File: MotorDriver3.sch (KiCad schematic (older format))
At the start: 38 parts, among them J22 43045-0802, J23 53426-0410, U45 MAX40056FAUA+, U46 DRV8312DDWR, U47 MAX40056FAUA+, U48 MIC2090-2YM5-TR

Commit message: PVT
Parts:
- C183: renamed from C191; footprint Capacitor-Chip:C_CHIP_1608_Reflow -> Capacitor-Chip:C_CHIP_1005_Hand_NoSilk; PartName GRM188R61E105KA12D -> TMK105BJ105MV-F
- C184: renamed from C192; PartName C1005X5R1V105K050BE -> TMK105BJ105MV-F
- C185: renamed from C193; PartName C1005X5R1V105K050BE -> TMK105BJ105MV-F
- C186: renamed from C194; footprint Capacitor-Chip:C_CHIP_1608_Reflow -> Capacitor-Chip:C_CHIP_1005_Hand_NoSilk; PartName GRM188R61E105KA12D -> TMK105BJ105MV-F
- C187: renamed from C195; footprint Capacitor-Chip:C_CHIP_1608_Reflow -> Capacitor-Chip:C_CHIP_1005_Hand_NoSilk; PartName GRM188R61E105KA12D -> TMK105BJ105MV-F
- C188: renamed from C196; footprint Capacitor-Chip:C_CHIP_1608_Reflow -> Capacitor-Chip:C_CHIP_1005_Hand_NoSilk; PartName GRM188R61E105KA12D -> TMK105BJ105MV-F
- C190: renamed from C198; PartName C1005X5R1V105K050BE -> TMK105BJ105MV-F
- C191: renamed from C199; PartName C1005X5R1V105K050BE -> TMK105BJ105MV-F
- C199: renamed from C207; PartName C1005X5R1V105K050BE -> TMK105BJ105MV-F
- R102: renamed from R117; value 2m -> 3m; PartName PMR18EZPJV2L0 -> PMR18EZPFV3L00
- R103: renamed from R118; value 2m -> 3m; PartName PMR18EZPJV2L0 -> PMR18EZPFV3L00
- renumbered C197 to C189, C200 to C192, C201 to C193, C202 to C194, C203 to C195, C204 to C196, C205 to C197, C206 to C198, L19 to L15, L20 to L16, L21 to L17, R115 to R100, R116 to R101, R119 to R104, R120 to R105, R113 to R98, R114 to R99, RA24 to RA25, RA25 to RA26, RA26 to RA27, U45 to U42, U46 to U43, U47 to U44, U48 to U45

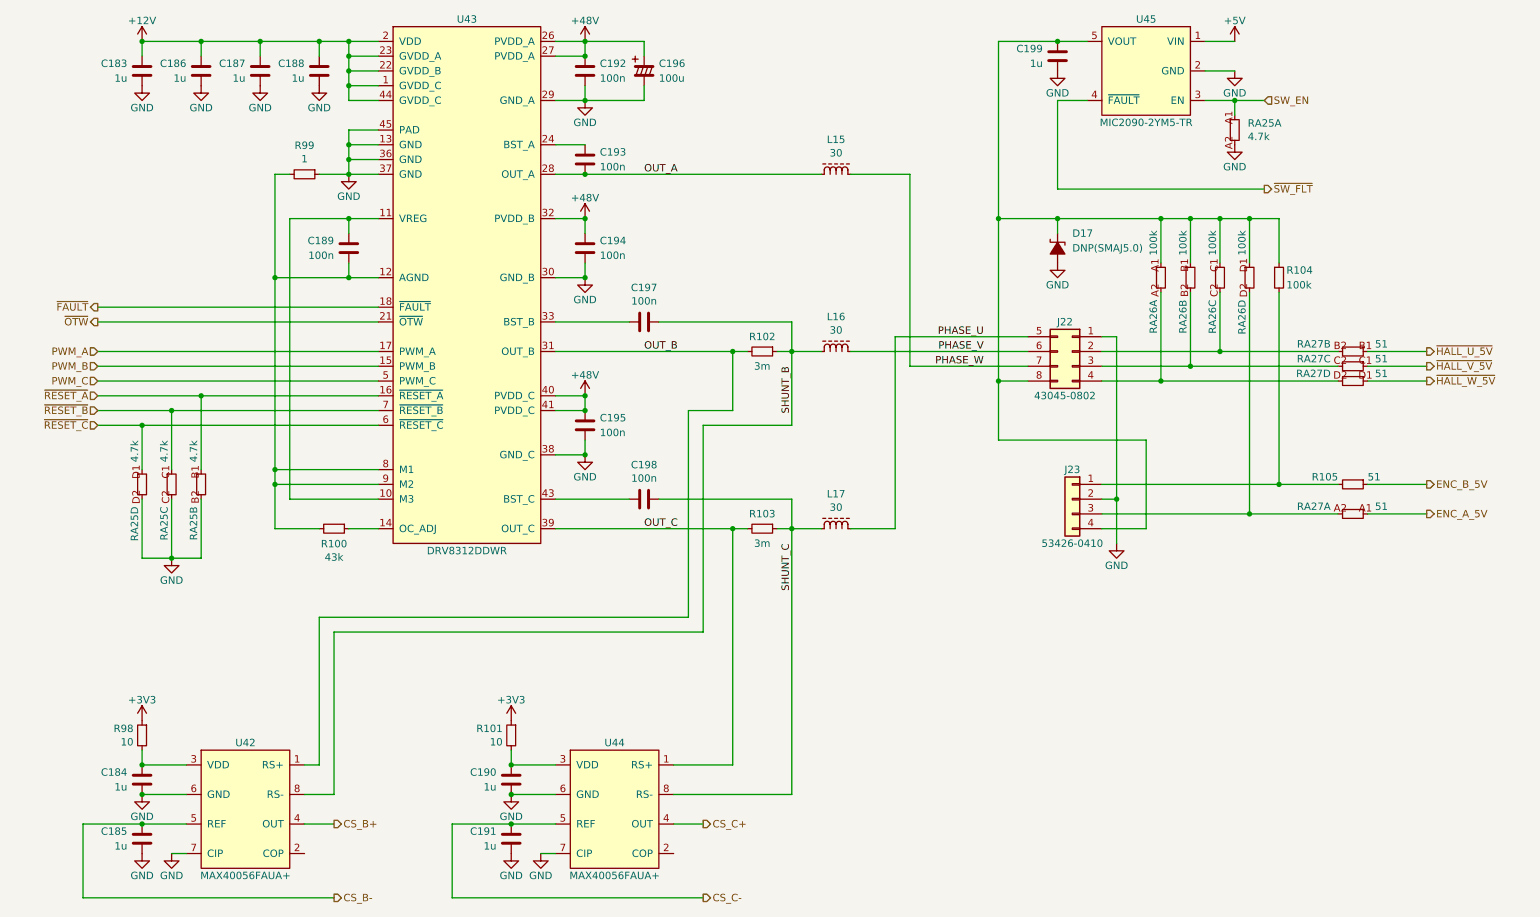
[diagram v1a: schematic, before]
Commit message: SBUにTVSダイオードを追加
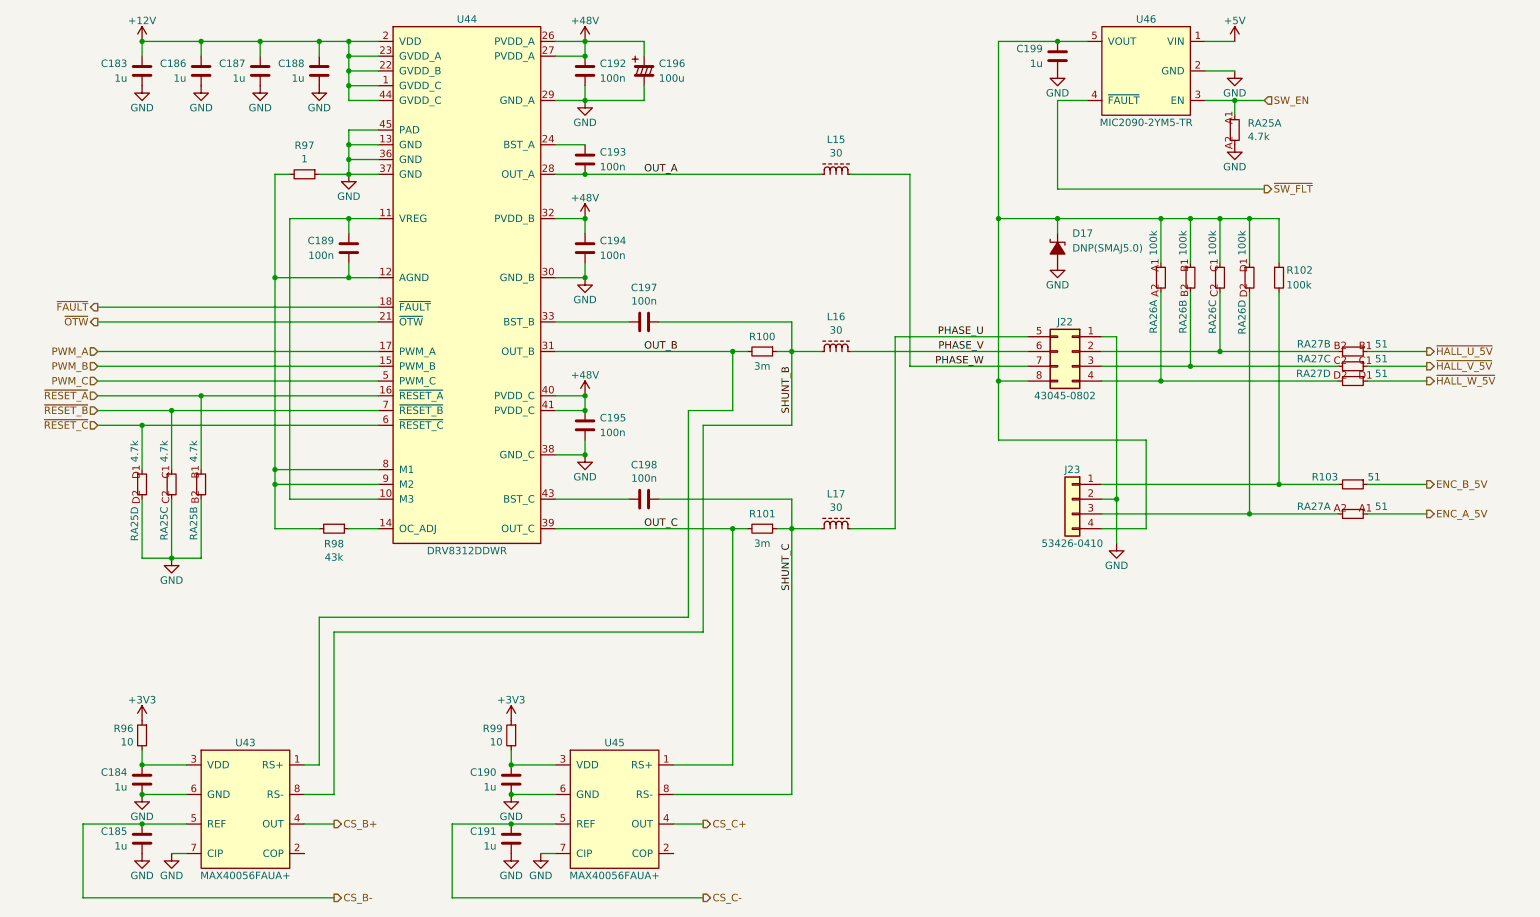
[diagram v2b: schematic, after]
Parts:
- renumbered R102 to R100, R103 to R101, R104 to R102, R105 to R103, R98 to R96, R99 to R97, R100 to R98, R101 to R99, U42 to U43, U43 to U44, U44 to U45, U45 to U46
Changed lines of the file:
@@
 AR Path="/5F237486/5E603889" Ref="U?"  Part="1"
 AR Path="/5F259EEE/5E603889" Ref="U?"  Part="1"
-AR Path="/5F259F40/5E603889" Ref="U43"  Part="1"
-F 0 "U43" H 4000 4750 50  0000 C CNN
+AR Path="/5F259F40/5E603889" Ref="U44"  Part="1"
+F 0 "U44" H 4000 4750 50  0000 C CNN
 F 1 "DRV8312DDWR" H 4000 1150 50  0000 C CNN
 F 2 "IC-SOP:HTSSOP44-W6.1_EP4.31x8.26" H 4000 2900 50  0001 C CNN
@@
 AR Path="/5F237486/5E603979" Ref="R?"  Part="1"
 AR Path="/5F259EEE/5E603979" Ref="R?"  Part="1"
-AR Path="/5F259F40/5E603979" Ref="R99"  Part="1"
-F 0 "R99" V 2705 2100 50  0000 C CNN
+AR Path="/5F259F40/5E603979" Ref="R97"  Part="1"
+F 0 "R97" V 2705 2100 50  0000 C CNN
 F 1 "1" V 2796 2100 50  0000 C CNN
 F 2 "Resistor-Chip:R_CHIP_1005_Hand_NoSilk" V 2950 2000 50  0001 C CNN
@@
 AR Path="/5F237486/5E603983" Ref="R?"  Part="1"
 AR Path="/5F259EEE/5E603983" Ref="R?"  Part="1"
-AR Path="/5F259F40/5E603983" Ref="R100"  Part="1"
-F 0 "R100" V 3203 4500 50  0000 C CNN
+AR Path="/5F259F40/5E603983" Ref="R98"  Part="1"
+F 0 "R98" V 3203 4500 50  0000 C CNN
 F 1 "43k" V 3294 4500 50  0000 C CNN
 F 2 "Resistor-Chip:R_CHIP_1005_Hand_NoSilk" V 3150 4400 50  0001 C CNN
@@
 AR Path="/5F237486/5E603998" Ref="R?"  Part="1"
 AR Path="/5F259EEE/5E603998" Ref="R?"  Part="1"
-AR Path="/5F259F40/5E603998" Ref="R103"  Part="1"
-F 0 "R103" V 5900 4500 50  0000 C CNN
+AR Path="/5F259F40/5E603998" Ref="R101"  Part="1"
+F 0 "R101" V 5900 4500 50  0000 C CNN
 F 1 "3m" V 6100 4500 50  0000 C CNN
 F 2 "Resistor-Chip:R_CHIP_3216_Reflow" V 6050 4400 50  0001 C CNN
@@
 AR Path="/5F237486/5E6039A5" Ref="R?"  Part="1"
 AR Path="/5F259EEE/5E6039A5" Ref="R?"  Part="1"
-AR Path="/5F259F40/5E6039A5" Ref="R102"  Part="1"
-F 0 "R102" V 5900 3300 50  0000 C CNN
+AR Path="/5F259F40/5E6039A5" Ref="R100"  Part="1"
+F 0 "R100" V 5900 3300 50  0000 C CNN
 F 1 "3m" V 6100 3300 50  0000 C CNN
 F 2 "Resistor-Chip:R_CHIP_3216_Reflow" V 6050 3200 50  0001 C CNN
@@
 AR Path="/5F235A43/5F1B2B35" Ref="U?"  Part="1"
 AR Path="/5F259EEE/5F1B2B35" Ref="U?"  Part="1"
-AR Path="/5F259F40/5F1B2B35" Ref="U45"  Part="1"
-F 0 "U45" H 8600 1750 50  0000 C CNN
+AR Path="/5F259F40/5F1B2B35" Ref="U46"  Part="1"
+F 0 "U46" H 8600 1750 50  0000 C CNN
 F 1 "MIC2090-2YM5-TR" H 8600 1050 50  0000 C CNN
 F 2 "IC-SOT:SOT23-5" H 8600 1400 50  0001 C CNN
@@
 AR Path="/5F235A43/5F4CEC4A" Ref="U?"  Part="1"
 AR Path="/5F237486/5F4CEC4A" Ref="U?"  Part="1"
-AR Path="/5F259F40/5F4CEC4A" Ref="U42"  Part="1"
-F 0 "U42" H 2500 6850 50  0000 C CNN
+AR Path="/5F259F40/5F4CEC4A" Ref="U43"  Part="1"
+F 0 "U43" H 2500 6850 50  0000 C CNN
 F 1 "MAX40056FAUA+" H 2500 5950 50  0000 C CNN
 F 2 "IC-SOP:MSOP8" H 2500 6400 50  0001 C CNN
@@
 AR Path="/5F235A43/5F4CEC50" Ref="U?"  Part="1"
 AR Path="/5F237486/5F4CEC50" Ref="U?"  Part="1"
-AR Path="/5F259F40/5F4CEC50" Ref="U44"  Part="1"
-F 0 "U44" H 5000 6850 50  0000 C CNN
+AR Path="/5F259F40/5F4CEC50" Ref="U45"  Part="1"
+F 0 "U45" H 5000 6850 50  0000 C CNN
 F 1 "MAX40056FAUA+" H 5000 5950 50  0000 C CNN
 F 2 "IC-SOP:MSOP8" H 5000 6400 50  0001 C CNN
@@
 AR Path="/5F235A43/5F4CECB6" Ref="R?"  Part="1"
 AR Path="/5F237486/5F4CECB6" Ref="R?"  Part="1"
-AR Path="/5F259F40/5F4CECB6" Ref="R98"  Part="1"
-F 0 "R98" H 1858 5946 50  0000 L CNN
+AR Path="/5F259F40/5F4CECB6" Ref="R96"  Part="1"
+F 0 "R96" H 1858 5946 50  0000 L CNN
 F 1 "10" H 1858 5855 50  0000 L CNN
 F 2 "Resistor-Chip:R_CHIP_1005_Hand_NoSilk" V 1850 5800 50  0001 C CNN
@@
 AR Path="/5F235A43/5F4CECBC" Ref="R?"  Part="1"
 AR Path="/5F237486/5F4CECBC" Ref="R?"  Part="1"
-AR Path="/5F259F40/5F4CECBC" Ref="R101"  Part="1"
-F 0 "R101" H 4358 5946 50  0000 L CNN
+AR Path="/5F259F40/5F4CECBC" Ref="R99"  Part="1"
+F 0 "R99" H 4358 5946 50  0000 L CNN
 F 1 "10" H 4358 5855 50  0000 L CNN
 F 2 "Resistor-Chip:R_CHIP_1005_Hand_NoSilk" V 4350 5800 50  0001 C CNN
@@
 P 10000 4200
 AR Path="/5F235A43/5EA4A632" Ref="R?"  Part="1"
-AR Path="/5F259F40/5EA4A632" Ref="R105"  Part="1"
-F 0 "R105" V 9950 4100 50  0000 R CNN
+AR Path="/5F259F40/5EA4A632" Ref="R103"  Part="1"
+F 0 "R103" V 9950 4100 50  0000 R CNN
 F 1 "51" V 9950 4300 50  0000 L CNN
 F 2 "Resistor-Chip:R_CHIP_1005_Hand_NoSilk" V 10050 4100 50  0001 C CNN
@@
 P 9500 2800
 AR Path="/5F235A43/5EA7860E" Ref="R?"  Part="1"
-AR Path="/5F259F40/5EA7860E" Ref="R104"  Part="1"
-F 0 "R104" H 9550 2850 50  0000 L CNN
+AR Path="/5F259F40/5EA7860E" Ref="R102"  Part="1"
+F 0 "R102" H 9550 2850 50  0000 L CNN
 F 1 "100k" H 9550 2750 50  0000 L CNN
 F 2 "Resistor-Chip:R_CHIP_1005_Hand_NoSilk" V 9550 2700 50  0001 C CNN
